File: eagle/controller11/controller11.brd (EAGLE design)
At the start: 30 x 65 mm, 61 parts, among them IC1 ILD213T, J2 AVR_SPI_PRG_62X3_LOCK, Q2 200mA/50V, Q4 200mA/50V, Q5 200mA/50V, U3 MP2307, X1 1501_04, X2 ZX62D-B-5PA8

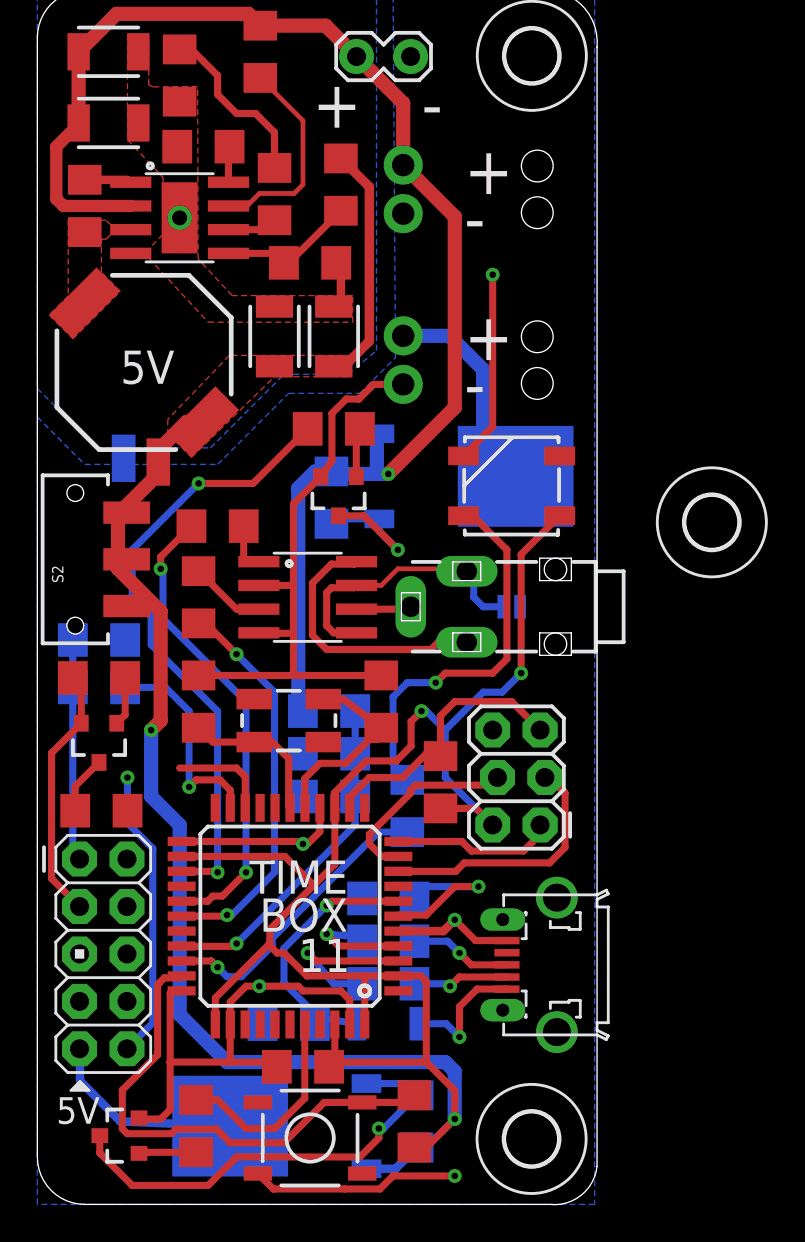
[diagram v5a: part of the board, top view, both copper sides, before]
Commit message: controller11: fixed silkscreen
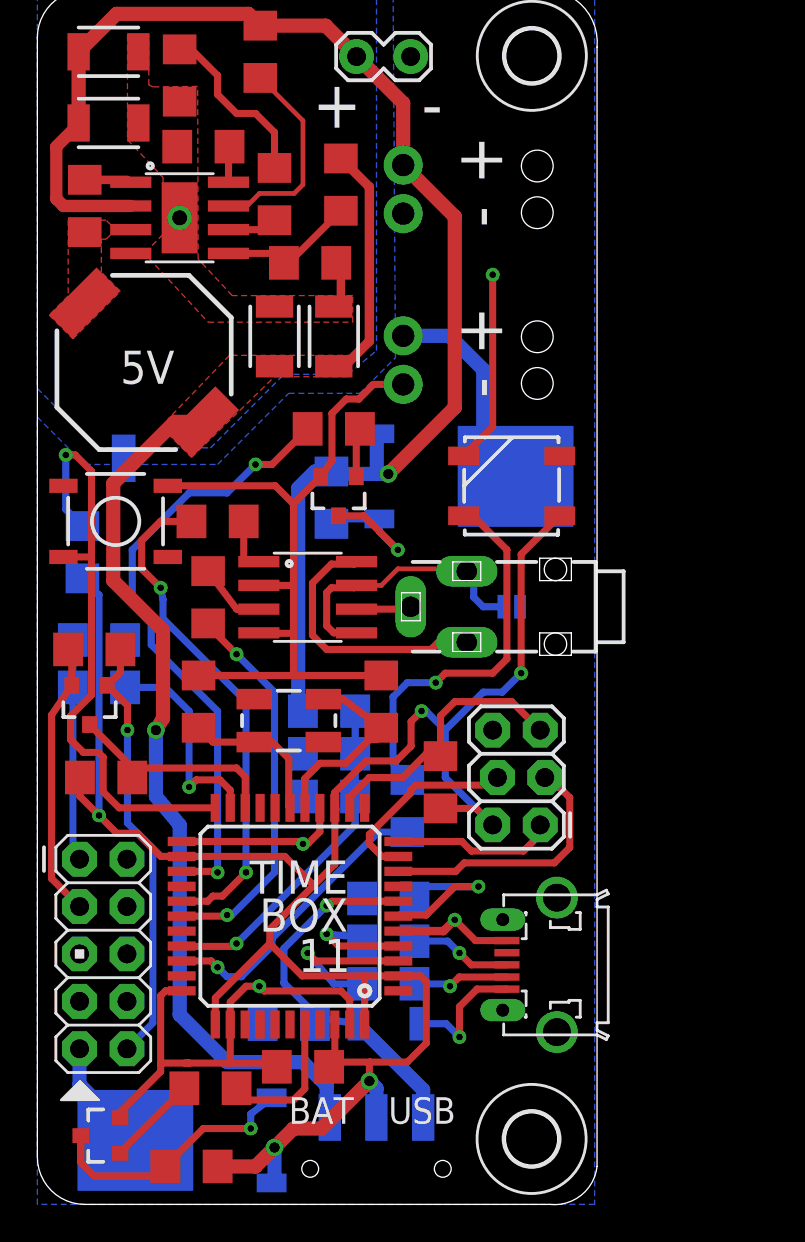
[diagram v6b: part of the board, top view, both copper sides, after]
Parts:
- removed H3: MOUNT-HOLE2.8, holes:2,8
- removed SH1: SHORT-HT5, shorts:SHORT_TOP-50
- moved S2 36.4 mm to (18.2, 1.91), flipped to the bottom, turned to 180 degrees
- moved R5 35.3 mm to (2.41, 34.9), flipped to the bottom
- moved S1 34.6 mm to (4.19, 36.6), turned to 0 degrees
- moved R4 12.3 mm to (8.26, 2.03), flipped to the top, turned to 180 degrees
- moved Q3 5.14 mm to (7.75, 3.43)
- moved R6 2.17 mm to (9.27, 6.22), turned to 180 degrees
- moved Q5 2.09 mm to (2.79, 26.8)
- moved R8 1.80 mm to (3.68, 22.9), turned to 0 degrees
- moved R7 1.55 mm to (3.05, 29.7)
- moved Q4 1.02 mm to (3.43, 3.68)
- moved R15 0.51 mm to (9.14, 32.5)
- moved R20 0.25 mm to (9.65, 36.6)
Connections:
- removed net N$22: C3.1, F2.2, U$3.7
- new net VBUS: C3.1, F2.2, S2.3, U$3.7
- net BTN: now also U$3.22; no longer U$3.32
- net CONV_5V: now also S2.1; no longer SH1.1
- net FOO5: now also U$3.32; no longer U$3.22
- net VCC: now also S2.2; no longer SH1.2
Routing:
- net CONV_5V: track 16.7 -> 61.4 mm, vias 0 -> 1
- net VCC: track 143.1 -> 116.0 mm, vias 4 -> 5
- net VBUS: track 0.00 -> 20.8 mm, vias 0 -> 1
- net N$22: track 14.3 -> 0.00 mm, vias 1 -> 0
- net N$3: track 23.9 -> 14.1 mm
- net BTN: track 27.2 -> 33.5 mm, vias 0 -> 1
- net ZERO_3.3V: track 18.3 -> 23.3 mm
- net ZERO_5V: track 10.7 -> 6.18 mm
- net GND: track 98.1 -> 94.6 mm, vias 5 -> 4
- net ZERO_EN: track 11.1 -> 7.61 mm
- net RX: track 8.48 -> 11.7 mm
- net CAM1: track 25.2 -> 27.2 mm
- net N$2: track 3.07 -> 4.92 mm
- net ZERO_TX: track 13.7 -> 14.8 mm
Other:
- board text added: "BAT"
- board text added: "IN"
- board text added: "OUT"
- board text added: "USB"
